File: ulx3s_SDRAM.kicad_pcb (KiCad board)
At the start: 4 copper layers, 14 parts, among them IC4 STM32F769IIT6, IC7 IS42S16400J

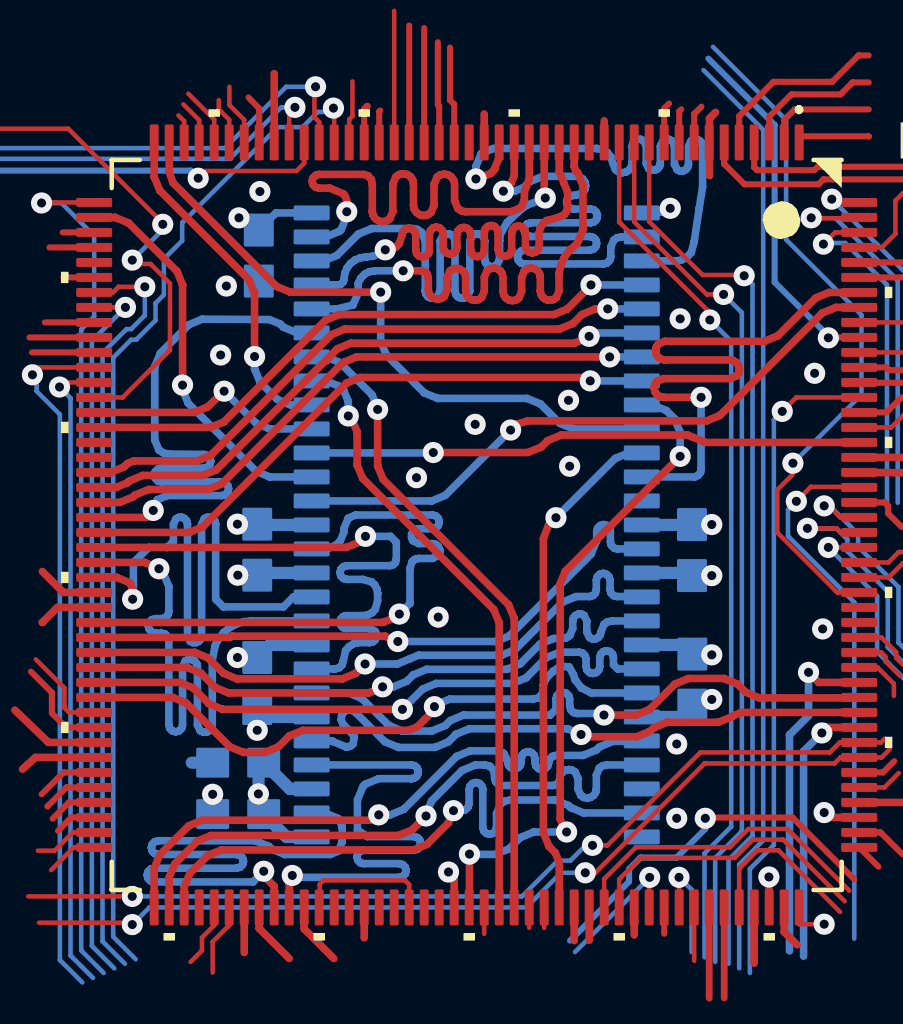
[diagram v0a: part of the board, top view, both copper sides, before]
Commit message: SDRAM footprint change
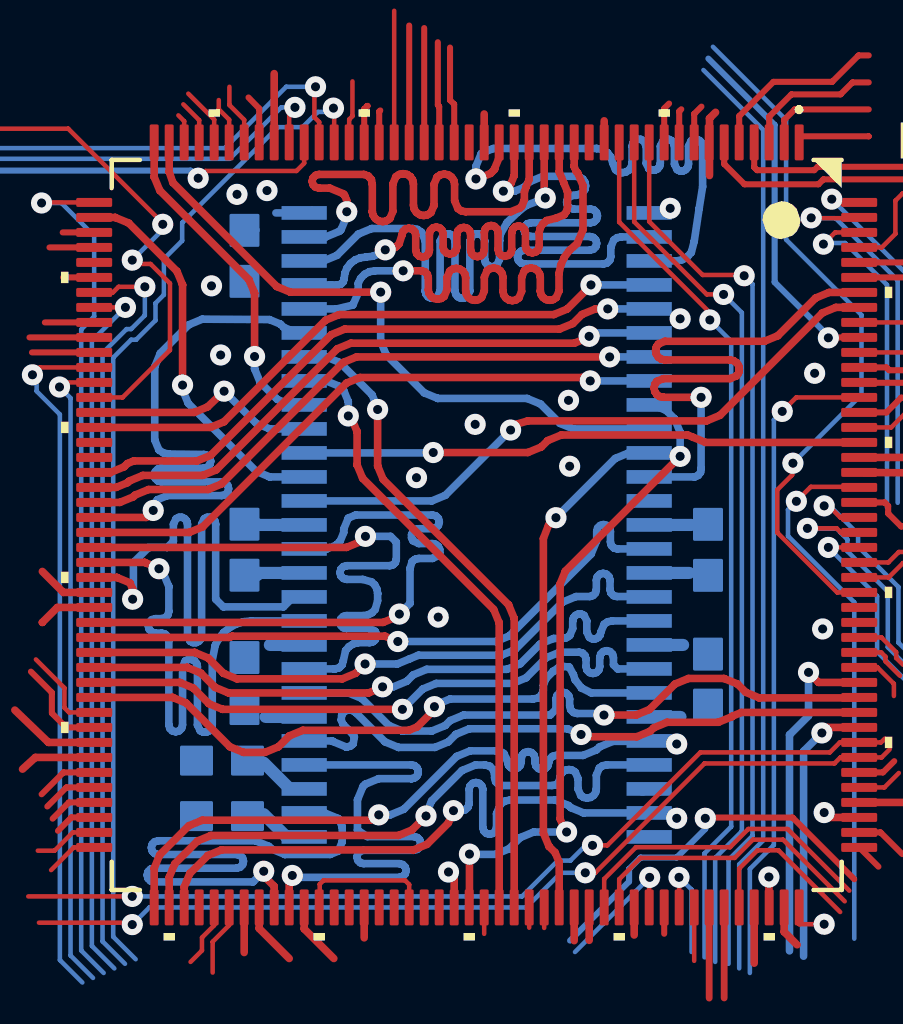
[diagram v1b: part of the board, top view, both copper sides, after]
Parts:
- IC7: footprint EEZ DIB MCU r3B4:TSOPII-54 -> Package_SO:TSOP-II-54_22.2x10.16mm_P0.8mm
- moved C49 0.54 mm to (0.08, 135.5)
- moved C43 0.54 mm to (0.08, 137.3)
- moved C47 0.53 mm to (16.3, 128.5)
- moved C48 0.52 mm to (16.3, 132.8)
- moved C46 0.48 mm to (0.83, 118.7)
- moved C44 0.42 mm to (0.83, 132.9)
- moved C45 0.42 mm to (0.83, 128.5)
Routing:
- net +3V3: track 43.0 -> 36.1 mm, vias 8 -> 3
- net GND: track 30.1 -> 25.2 mm, vias 22 -> 17

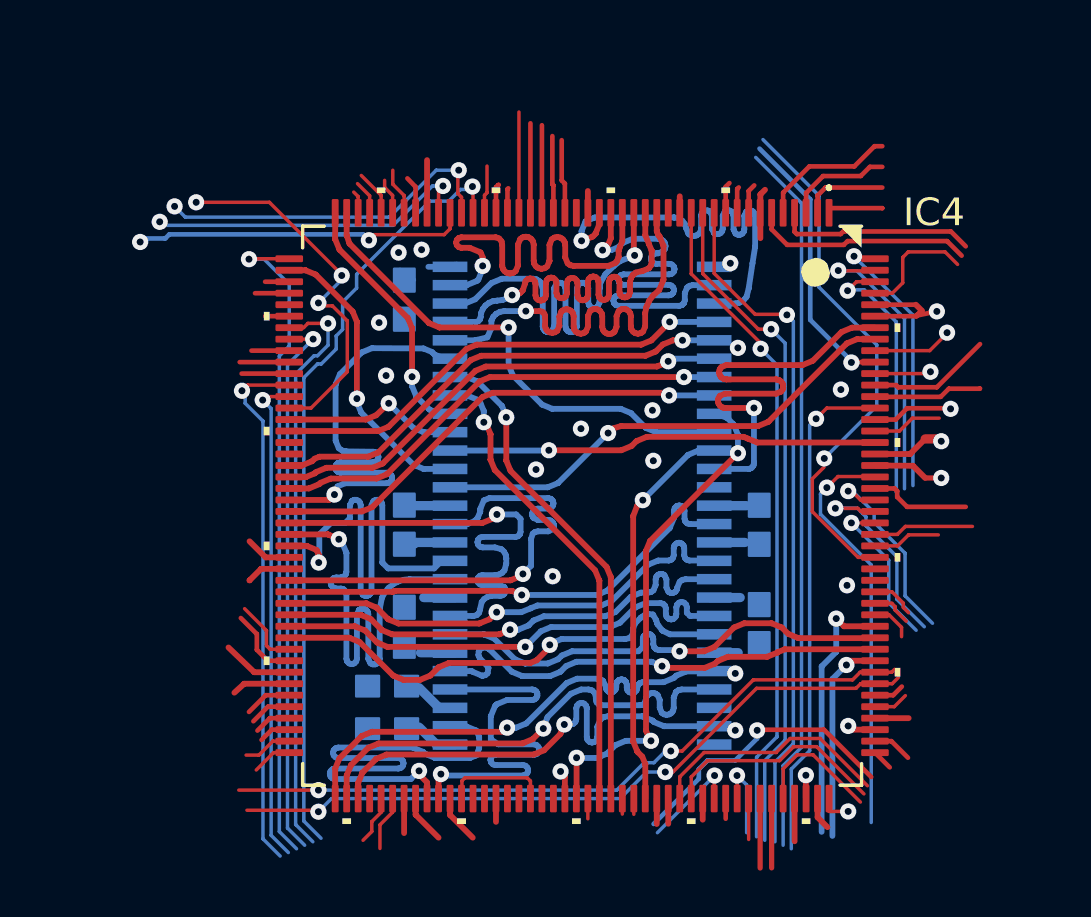
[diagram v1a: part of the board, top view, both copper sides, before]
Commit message: STM32 footprint change
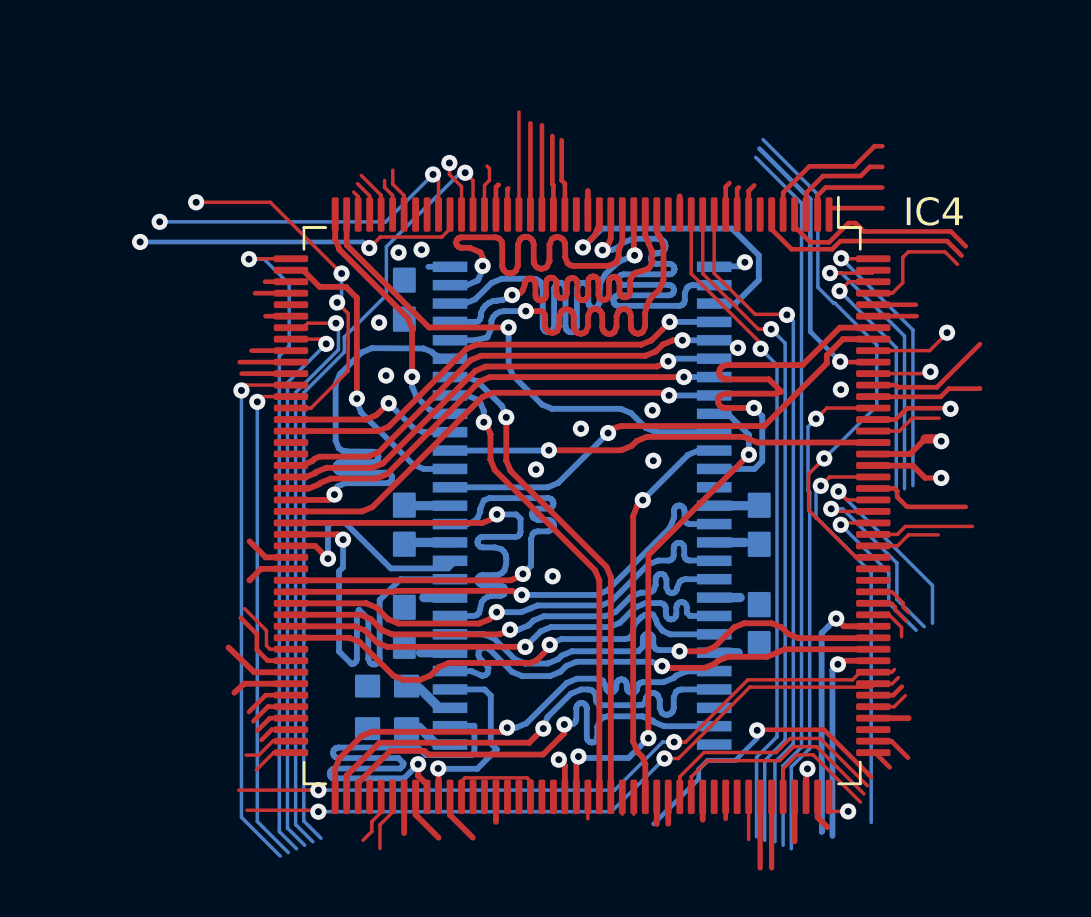
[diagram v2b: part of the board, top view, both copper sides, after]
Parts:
- IC4: footprint EEZ DIB MCU r3B4:LQFP-176_24X24MM -> Package_QFP:LQFP-176_24x24mm_P0.5mm
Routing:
- net ETH_MDC: track 15.4 -> 2.39 mm, vias 2 -> 1
- net FMC_D6: track 20.8 -> 10.1 mm
- net FMC_D1: track 18.9 -> 8.33 mm
- net FMC_A5: track 20.1 -> 14.0 mm
- net +3V3: track 36.1 -> 30.7 mm, vias 3 -> 2
- net MCLK_25: track 4.53 -> 0.00 mm, vias 1 -> 0
- net GND: track 25.2 -> 21.5 mm, vias 17 -> 14
- net USB_OTG_FS_VBUS: track 3.67 -> 0.00 mm, vias 1 -> 0
- net ~FAULT: track 16.3 -> 15.4 mm
- net FMC_D5: track 20.8 -> 20.0 mm
- net LTDC_G2: track 23.8 -> 24.5 mm
- net LTDC_B7: track 12.0 -> 12.7 mm
- net LTDC_G3: track 6.87 -> 7.47 mm
- net FMC_SDNWE: track 13.0 -> 13.6 mm
- net LTDC_R5: track 33.7 -> 34.2 mm
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
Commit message: Partial copied SDRAM routing from BB3
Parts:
- removed C47: 100n, EEZ DIB MCU r3B4:C0603
- removed IC4: STM32F769IIT6, Package_QFP:LQFP-176_24x24mm_P0.5mm
- removed IC7: IS42S16400J, Package_SO:TSOP-II-54_22.2x10.16mm_P0.8mm
- added B101: DS1092-10-W6L, EEZ DIB MCU r3B4:DS1092-10-W6L, F.Cu at (241.3, 39.5)
- added C1: 22uF, Capacitor_SMD:C_0805_2012Metric, B.Cu at (197.5, 75.9)
- added C10: 470pF, Capacitor_SMD:C_0603_1608Metric, B.Cu at (191.9, 76.7)
- added C101: N.C., Capacitor_SMD:C_0805_2012Metric, F.Cu at (139.9, 61.8)
- added C102: EEEFK1V220R, EEZ DIB MCU r3B4:PANASONIC_C, F.Cu at (249.8, 99.0)
- added C103: 2u2, Capacitor_SMD:C_0805_2012Metric, F.Cu at (252.7, 62.4)
- added C104: 10n, Capacitor_SMD:C_0805_2012Metric, F.Cu at (254.8, 111.1)
- added C105: 100n, Capacitor_SMD:C_0603_1608Metric, F.Cu at (169.4, 109.5)
- added C106: 10n, Capacitor_SMD:C_0805_2012Metric, F.Cu at (235.1, 106.1)
- added C107: 100n, Capacitor_SMD:C_0603_1608Metric, F.Cu at (168.9, 102.3)
- added C108: 10n, Capacitor_SMD:C_0805_2012Metric, F.Cu at (232.4, 106.1)
- added C109: 10n, Capacitor_SMD:C_0805_2012Metric, F.Cu at (241.0, 106.1)
- added C11: 22uF, Capacitor_SMD:C_0805_2012Metric, B.Cu at (191.9, 73.5)
- added C110: 100n, Capacitor_SMD:C_0603_1608Metric, F.Cu at (242.8, 105.8)
- added C111: 33p, Capacitor_SMD:C_0603_1608Metric, F.Cu at (160.0, 63.5)
- added C112: 4p7, Capacitor_SMD:C_0603_1608Metric, F.Cu at (171.3, 63.5)
- added C113: 33p, Capacitor_SMD:C_0603_1608Metric, F.Cu at (156.6, 63.5)
- added C114: 4p7, Capacitor_SMD:C_0603_1608Metric, F.Cu at (168.1, 63.5)
- added C115: EEEFK1V220R, EEZ DIB MCU r3B4:PANASONIC_C, F.Cu at (138.8, 107.4)
- added C116: 100n, Capacitor_SMD:C_0603_1608Metric, F.Cu at (144.2, 107.9)
- added C117: 100n, Capacitor_SMD:C_0603_1608Metric, B.Cu at (165.5, 63.8)
- added C118: 100n, Capacitor_SMD:C_0603_1608Metric, F.Cu at (179.8, 71.1)
- added C119: 100n, Capacitor_SMD:C_0603_1608Metric, F.Cu at (179.0, 78.6)
- added C12: 22uF, Capacitor_SMD:C_0805_2012Metric, B.Cu at (191.9, 71.6)
- added C120: 100n, Capacitor_SMD:C_0603_1608Metric, F.Cu at (183.3, 84.0)
- added C121: 100n, Capacitor_SMD:C_0603_1608Metric, F.Cu at (183.2, 90.4)
- added C122: 100n, Capacitor_SMD:C_0603_1608Metric, F.Cu at (176.9, 95.9)
- added C123: 100n, Capacitor_SMD:C_0603_1608Metric, F.Cu at (187.9, 59.3)
- added C124: 100n, Capacitor_SMD:C_0603_1608Metric, F.Cu at (165.2, 96.4)
- added C125: 1u, Capacitor_SMD:C_0805_2012Metric, F.Cu at (165.2, 98.2)
- added C126: 100n, Capacitor_SMD:C_0603_1608Metric, F.Cu at (158.4, 99.2)
- added C127: 100n, Capacitor_SMD:C_0603_1608Metric, F.Cu at (155.2, 99.2)
- added C128: 100n, Capacitor_SMD:C_0603_1608Metric, F.Cu at (141.9, 89.3)
- added C129: 100n, Capacitor_SMD:C_0603_1608Metric, F.Cu at (142.5, 83.6)
- added C13: 2.2uF, Capacitor_SMD:C_0805_2012Metric, F.Cu at (203.1, 69.9)
- added C130: 100n, Capacitor_SMD:C_0603_1608Metric, F.Cu at (142.4, 79.9)
- added C131: 100n, Capacitor_SMD:C_0603_1608Metric, B.Cu at (154.1, 64.4)
- added C132: 2u2, Capacitor_SMD:C_0805_2012Metric, F.Cu at (150.6, 109.0)
- added C133: 2u2, Capacitor_SMD:C_0805_2012Metric, B.Cu at (163.0, 63.9)
- added C134: 100n, Capacitor_SMD:C_0603_1608Metric, F.Cu at (143.6, 75.3)
- added C135: 1u, Capacitor_SMD:C_0805_2012Metric, F.Cu at (143.4, 73.5)
- added C136: 1u, Capacitor_SMD:C_0805_2012Metric, F.Cu at (151.0, 62.4)
- added C137: 100n, Capacitor_SMD:C_0603_1608Metric, F.Cu at (147.5, 62.4)
- added C138: 2u2, Capacitor_SMD:C_0805_2012Metric, F.Cu at (172.9, 97.7)
- added C139: 2u2, Capacitor_SMD:C_0805_2012Metric, F.Cu at (141.5, 87.3)
- added C140: N.C., Capacitor_SMD:C_0603_1608Metric, B.Cu at (232.4, 50.8)
- added C141: 4u7, Capacitor_SMD:C_1206_3216Metric, B.Cu at (179.3, 119.2)
- added C142: 100n, Capacitor_SMD:C_0603_1608Metric, B.Cu at (183.2, 80.4)
- added C143: 100n, Capacitor_SMD:C_0603_1608Metric, B.Cu at (87.5, 93.2)
- added C144: 100n, Capacitor_SMD:C_0603_1608Metric, B.Cu at (88.2, 88.9)
- added C145: 100n, Capacitor_SMD:C_0603_1608Metric, B.Cu at (88.2, 84.4)
- added C146: 100n, Capacitor_SMD:C_0603_1608Metric, B.Cu at (88.3, 74.6)
- added C147: 100n, Capacitor_SMD:C_0603_1608Metric, B.Cu at (103.6, 84.5)
- added C148: 100n, Capacitor_SMD:C_0603_1608Metric, B.Cu at (103.6, 88.8)
- added C149: 100n, Capacitor_SMD:C_0603_1608Metric, B.Cu at (87.5, 91.5)
- added C150: 4u7, Capacitor_SMD:C_1206_3216Metric, F.Cu at (132.6, 98.6)
- added C151: 1u, Capacitor_SMD:C_0805_2012Metric, F.Cu at (180.0, 103.6)
- added C152: 4u7, Capacitor_Tantalum_SMD:CP_EIA-3216-10_Kemet-I, F.Cu at (218.9, 106.5)
- added C153: 2u2, Capacitor_SMD:C_0805_2012Metric, F.Cu at (182.4, 103.6)
- added C154: 4n7/1kV, Capacitor_SMD:C_1812_4532Metric, F.Cu at (219.1, 121.1)
- added C155: 100n, Capacitor_SMD:C_0603_1608Metric, F.Cu at (212.0, 112.4)
- added C156: 4u7, Capacitor_SMD:C_1206_3216Metric, F.Cu at (195.6, 39.0)
- added C157: 100n, Capacitor_SMD:C_0603_1608Metric, F.Cu at (183.8, 96.2)
- added C158: 1u, Capacitor_SMD:C_0805_2012Metric, F.Cu at (183.8, 99.7)
- added C159: N.C., Capacitor_SMD:C_0603_1608Metric, F.Cu at (136.6, 44.1)
- added C160: 100n, Capacitor_SMD:C_0603_1608Metric, F.Cu at (153.2, 36.9)
- added C161: 100n, Capacitor_SMD:C_0603_1608Metric, F.Cu at (134.6, 45.2)
- added C162: 100n, Capacitor_SMD:C_0603_1608Metric, F.Cu at (158.9, 37.1)
- added C163: 100n, Capacitor_SMD:C_0603_1608Metric, F.Cu at (134.8, 36.7)
- added C164: 100n, Capacitor_SMD:C_0603_1608Metric, F.Cu at (156.8, 53.6)
- added C165: 100n, Capacitor_SMD:C_0603_1608Metric, F.Cu at (147.4, 33.9)
- added C166: 10uF, Capacitor_Tantalum_SMD:CP_EIA-3216-10_Kemet-I, F.Cu at (148.1, 52.2)
- added C167: 100n, Capacitor_SMD:C_0603_1608Metric, F.Cu at (146.3, 48.9)
- added C168: 100n, Capacitor_SMD:C_0603_1608Metric, F.Cu at (143.8, 42.0)
- added C169: 100n, Capacitor_SMD:C_0603_1608Metric, F.Cu at (154.6, 53.6)
- added C17: 2.2uF, Capacitor_SMD:C_0805_2012Metric, B.Cu at (213.5, 89.7)
- added C170: 100n, Capacitor_SMD:C_0603_1608Metric, F.Cu at (160.5, 43.8)
- added C19: 2.2uF, Capacitor_SMD:C_0805_2012Metric, B.Cu at (213.5, 79.5)
- added C2: 470pF, Capacitor_SMD:C_0603_1608Metric, B.Cu at (229.9, 95.0)
- added C20: 2.2uF, Capacitor_SMD:C_0805_2012Metric, B.Cu at (213.5, 84.7)
- added C22: 2.2uF, Capacitor_SMD:C_0805_2012Metric, B.Cu at (230.4, 96.6)
- added C23: 2.2uF, Capacitor_SMD:C_0805_2012Metric, B.Cu at (194.7, 66.4)
- added C24: 2.2uF, Capacitor_SMD:C_0805_2012Metric, B.Cu at (225.3, 73.0)
- added C25: 22nF, Capacitor_SMD:C_0603_1608Metric, B.Cu at (215.9, 84.3)
- added C26: 22nF, Capacitor_SMD:C_0603_1608Metric, B.Cu at (211.1, 84.3)
- added C27: 22nF, Capacitor_SMD:C_0603_1608Metric, B.Cu at (211.9, 89.3)
- added C28: 22nF, Capacitor_SMD:C_0603_1608Metric, B.Cu at (215.1, 89.3)
- added C29: 22nF, Capacitor_SMD:C_0603_1608Metric, B.Cu at (217.0, 89.2)
- added C3: 22uF, Capacitor_SMD:C_0805_2012Metric, B.Cu at (230.1, 88.7)
- added C30: 22nF, Capacitor_SMD:C_0603_1608Metric, B.Cu at (209.9, 89.1)
- added C31: 22nF, Capacitor_SMD:C_0603_1608Metric, B.Cu at (211.1, 86.5)
- added C32: 22nF, Capacitor_SMD:C_0603_1608Metric, B.Cu at (215.9, 86.5)
- added C36: 220nF, Capacitor_SMD:C_0603_1608Metric, F.Cu at (225.4, 73.9)
- added C37: 220nF, Capacitor_SMD:C_0603_1608Metric, F.Cu at (226.8, 73.9)
- added C38: 220nF, Capacitor_SMD:C_0603_1608Metric, F.Cu at (215.2, 73.9)
- added C39: 220nF, Capacitor_SMD:C_0603_1608Metric, F.Cu at (218.0, 73.9)
- added C4: 22uF, Capacitor_SMD:C_0805_2012Metric, B.Cu at (230.1, 90.6)
- added C40: 220nF, Capacitor_SMD:C_0603_1608Metric, F.Cu at (220.8, 73.9)
- added C41: 220nF, Capacitor_SMD:C_0603_1608Metric, F.Cu at (224.0, 73.9)
- added C42: 220nF, Capacitor_SMD:C_0603_1608Metric, F.Cu at (213.8, 73.9)
- added C5: 22uF, Capacitor_SMD:C_0805_2012Metric, B.Cu at (238.4, 90.0)
- added C50: 22nF, Capacitor_SMD:C_0603_1608Metric, B.Cu at (238.2, 82.7)
- added C51: 22nF, Capacitor_SMD:C_0603_1608Metric, B.Cu at (237.7, 96.3)
- added C53: 22nF, Capacitor_SMD:C_0603_1608Metric, B.Cu at (199.4, 83.1)
- added C6: 470pF, Capacitor_SMD:C_0603_1608Metric, B.Cu at (227.6, 80.5)
- added C7: 22uF, Capacitor_SMD:C_0805_2012Metric, B.Cu at (227.6, 77.3)
- added C8: 22uF, Capacitor_SMD:C_0805_2012Metric, B.Cu at (227.6, 75.4)
- added C9: 22uF, Capacitor_SMD:C_0805_2012Metric, B.Cu at (235.8, 76.7)
- added D101: SMBJ5.0A-TR, EEZ DIB MCU r3B4:DO214AA, F.Cu at (139.8, 68.9)
- added D102: RB751V40T1G, EEZ DIB MCU r3B4:SOD323-R, F.Cu at (178.0, 103.2)
- added D20: 3.6V, Diode_SMD:D_SOD-323, B.Cu at (201.4, 39.9)
- added D21: 3.6V, Diode_SMD:D_SOD-323, B.Cu at (207.6, 39.8)
- added D23: 1N914, Diode_SMD:D_SOD-323, B.Cu at (202.4, 43.3)
- added D24: 1N914, Diode_SMD:D_SOD-323, B.Cu at (200.4, 43.3)
- added D25: 1N914, Diode_SMD:D_SOD-323, B.Cu at (206.6, 43.1)
- added D26: 1N914, Diode_SMD:D_SOD-323, B.Cu at (208.5, 43.1)
- added D28: 1N914, Diode_SMD:D_SOD-323, B.Cu at (230.4, 82.3)
- added D29: 1N914, Diode_SMD:D_SOD-323, B.Cu at (230.4, 84.1)
- added D9: 0, jumper:D_SMA_Jumper_NC, B.Cu at (202.9, 47.4)
- added FM1: FIDUCIAL, EEZ DIB MCU r3B4:FIDUCIAL, F.Cu at (263.5, 111.0)
- added FM2: FIDUCIAL, EEZ DIB MCU r3B4:FIDUCIAL, F.Cu at (130.5, 116.0)
- added FM3: FIDUCIAL, EEZ DIB MCU r3B4:FIDUCIAL, F.Cu at (131.0, 35.4)
- added FM4: FIDUCIAL, EEZ DIB MCU r3B4:FIDUCIAL, F.Cu at (263.4, 35.7)
- added GND1: PCB_TEST_TABSHIELD, EEZ DIB MCU r3B4:PCB_SHIELD_TAB, F.Cu at (222.2, 50.2)
- added GPDI1: GPDI-D, conn-fci:CONN-10029449-111RLF, F.Cu at (221.5, 40.0)
- added H1: HOLE, MountingHole:MountingHole_3.2mm_M3_ISO14580_Pad, F.Cu at (131.0, 57.5)
- added H2: HOLE, MountingHole:MountingHole_3.2mm_M3_ISO14580_Pad, F.Cu at (249.9, 57.5)
- added H3: HOLE, MountingHole:MountingHole_3.2mm_M3_ISO14580_Pad, F.Cu at (249.9, 120.5)
- added H4: HOLE, MountingHole:MountingHole_3.2mm_M3_ISO14580_Pad, F.Cu at (130.8, 120.5)
- added IC101: TPD4E001DRLR, EEZ DIB MCU r3B4:DRL6, F.Cu at (167.9, 111.5)
- added IC102: 74AUP1G74DC.125, EEZ DIB MCU r3B4:DCU8, F.Cu at (245.2, 106.1)
- added IC103: CD74HC4050PWR, EEZ DIB MCU r3B4:PW16, F.Cu at (157.2, 104.8)
- added IC104: STM32F769IIT6, Package_QFP:LQFP-176_24x24mm_P0.5mm, F.Cu at (95.9, 83.6)
- added IC105: LD1117ADT33TR, EEZ DIB MCU r3B4:DPACK, F.Cu at (145.8, 115.7)
- added IC106: N.C., EEZ DIB MCU r3B4:DRL6, B.Cu at (179.9, 57.2)
- added IC107: IS42S16400J, Package_SO:TSOP-II-54_22.2x10.16mm_P0.8mm, B.Cu at (95.9, 83.6)
- added IC108: AT24C256C-SSHL-B, EEZ DIB MCU r3B4:SOIC127P600X173-8N, B.Cu at (185.2, 76.7)
- added IC109: TPS2051BDBVR, EEZ DIB MCU r3B4:DBV5, F.Cu at (218.5, 110.9)
- added IC110: TPS61169DCKR, EEZ DIB MCU r3B4:DCK5, F.Cu at (133.4, 94.0)
- added IC111: TPD4E001DRLR, EEZ DIB MCU r3B4:DRL6, F.Cu at (209.0, 110.5)
- added IC112: TSC2007IPW, EEZ DIB MCU r3B4:PW(R-PDSO-G16), B.Cu at (205.3, 104.7)
- added IC113: N.C., EEZ DIB MCU r3B4:DRL6, F.Cu at (160.8, 41.3)
- added IC114: DP83848CVV_NOPB, EEZ DIB MCU r3B4:PT48, F.Cu at (153.6, 45.8)
- added J101: 503398-1892, EEZ DIB MCU r3B4:5033981892, B.Cu at (182.5, 109.8)
- added J102: 67803-8020, EEZ DIB MCU r3B4:678038020, F.Cu at (209.0, 123.0)
- added J4: CONN_02X03, Socket_Strips:Socket_Strip_Straight_2x03, F.Cu at (216.0, 101.4)
- added JP101: JP2-NOCUT, EEZ DIB MCU r3B4:JP2-NOCUT, F.Cu at (176.0, 58.8)
- added JP102: JP2-NOCUT, EEZ DIB MCU r3B4:JP2-NOCUT, F.Cu at (174.1, 58.8)
- added JP103: JP2-CUT-0805, EEZ DIB MCU r3B4:R_0805, F.Cu at (232.2, 47.3)
- added JP104: JP2-CUT-0805, EEZ DIB MCU r3B4:R_0805, F.Cu at (251.0, 90.4)
- added JP105: JP2-CUT, EEZ DIB MCU r3B4:JP2-CUT, B.Cu at (177.4, 59.0)
- added JP106: JP3-CUT-0805-ROTATED, EEZ DIB MCU r3B4:JP3-0805-CUT2, F.Cu at (188.7, 115.7)
- added JP107: JP2-NOCUT-0805, EEZ DIB MCU r3B4:JP2-0805-NOCUT, F.Cu at (205.5, 111.4)
- added JP108: JP2-CUT, EEZ DIB MCU r3B4:JP2-CUT, F.Cu at (139.9, 43.0)
- added JP109: JP2-CUT, EEZ DIB MCU r3B4:JP2-CUT, F.Cu at (139.9, 44.9)
- added JP110: JP2-CUT, EEZ DIB MCU r3B4:JP2-CUT, F.Cu at (139.9, 41.0)
- added JP111: JP2-NOCUT, EEZ DIB MCU r3B4:JP2-NOCUT, F.Cu at (139.9, 46.9)
- added JP112: JP2-NOCUT, EEZ DIB MCU r3B4:JP2-NOCUT, F.Cu at (163.0, 45.1)
- added L1: 2.2uH, L_1008_1210:L_1008_1210, B.Cu at (233.9, 86.2)
- added L101: BLM18AG102SH1D, EEZ DIB MCU r3B4:BEAD0603, F.Cu at (147.4, 64.4)
- added L102: DLG-0403-4R7, EEZ DIB MCU r3B4:DE0403, F.Cu at (174.3, 103.4)
- added L103: BLM18AG102SH1D, EEZ DIB MCU r3B4:BEAD0603, F.Cu at (142.8, 38.4)
- added L2: 2.2uH, L_1008_1210:L_1008_1210, B.Cu at (196.3, 69.1)
- added L3: 2.2uH, L_1008_1210:L_1008_1210, B.Cu at (231.4, 72.9)
- added LABEL1: HR000002, EEZ DIB MCU r3B4:CERT-SMALL-SILK, F.Cu at (248.6, 74.0)
- added LCD101: 505110-4091, EEZ DIB MCU r3B4:FPC_40, F.Cu at (189.6, 110.3)
- added LED101: N.C., EEZ DIB MCU r3B4:LED_0805, F.Cu at (222.7, 117.8)
- added LED102: N.C., EEZ DIB MCU r3B4:LED_0805, F.Cu at (190.2, 37.8)
- added Q101: N.C., EEZ DIB MCU r3B4:SOT23-BEC, F.Cu at (218.3, 115.6)
- added Q102: 2N7002, EEZ DIB MCU r3B4:SOT103P240X110-3N, F.Cu at (198.6, 52.4)
- added R101: 4K7, Resistor_SMD:R_0603_1608Metric, F.Cu at (228.5, 106.1)
- added R102: 10K, Resistor_SMD:R_0603_1608Metric, F.Cu at (230.5, 106.1)
- added R103: 10K, Resistor_SMD:R_0603_1608Metric, F.Cu at (249.9, 106.1)
- added R104: 4K7, Resistor_SMD:R_0603_1608Metric, F.Cu at (164.2, 107.4)
- added R105: 4K7, Resistor_SMD:R_0603_1608Metric, F.Cu at (164.2, 103.5)
- added R106: 1K, Resistor_SMD:R_0603_1608Metric, F.Cu at (141.9, 96.4)
- added R107: 4K7, Resistor_SMD:R_0603_1608Metric, F.Cu at (237.0, 106.1)
- added R108: 4K7, Resistor_SMD:R_0603_1608Metric, F.Cu at (166.7, 107.4)
- added R109: 4K7, Resistor_SMD:R_0603_1608Metric, F.Cu at (166.7, 103.5)
- added R11: 10k, Resistor_SMD:R_0603_1608Metric, B.Cu at (192.7, 96.3)
- added R110: 1K, Resistor_SMD:R_0603_1608Metric, F.Cu at (141.9, 94.5)
- added R111: 10K, Resistor_SMD:R_0603_1608Metric, F.Cu at (239.0, 106.1)
- added R112: 4K7, Resistor_SMD:R_0603_1608Metric, F.Cu at (160.8, 46.9)
- added R113: 10K, Resistor_SMD:R_0603_1608Metric, F.Cu at (143.4, 71.5)
- added R114: N.C., Resistor_SMD:R_0603_1608Metric, F.Cu at (247.9, 106.1)
- added R115: 4K7, Resistor_SMD:R_0603_1608Metric, F.Cu at (144.0, 66.2)
- added R116: 1K5, Resistor_SMD:R_0805_2012Metric, F.Cu at (192.5, 58.1)
- added R117: 1K5, Resistor_SMD:R_0805_2012Metric, F.Cu at (192.7, 60.5)
- added R118: 47R, Resistor_SMD:R_0805_2012Metric, F.Cu at (151.0, 64.3)
- added R119: N.C., Resistor_SMD:R_0805_2012Metric, B.Cu at (180.1, 66.4)
- added R12: 10k, Resistor_SMD:R_0603_1608Metric, B.Cu at (191.6, 99.1)
- added R120: N.C., Resistor_SMD:R_0805_2012Metric, B.Cu at (180.7, 94.8)
- added R121: N.C., Resistor_SMD:R_0805_2012Metric, B.Cu at (183.4, 87.0)
- added R122: 47K, Resistor_SMD:R_0603_1608Metric, B.Cu at (199.6, 115.4)
- added R123: 47K, Resistor_SMD:R_0603_1608Metric, B.Cu at (199.6, 119.2)
- added R124: 10R, Resistor_SMD:R_0603_1608Metric, F.Cu at (133.1, 96.4)
- added R125: N.C., Resistor_SMD:R_0603_1608Metric, F.Cu at (222.7, 115.9)
- added R126: 10R, Resistor_SMD:R_0603_1608Metric, F.Cu at (133.4, 91.5)
- added R127: 10K, Resistor_SMD:R_0603_1608Metric, F.Cu at (222.7, 112.0)
- added R128: N.C., Resistor_SMD:R_0603_1608Metric, F.Cu at (222.7, 113.9)
- added R129: 4K7, Resistor_SMD:R_0805_2012Metric, F.Cu at (212.4, 108.6)
- added R130: 22R, Resistor_SMD:R_0805_2012Metric, F.Cu at (168.8, 98.1)
- added R131: 22R, Resistor_SMD:R_0805_2012Metric, F.Cu at (170.7, 98.1)
- added R132: 10K, Resistor_SMD:R_0603_1608Metric, F.Cu at (212.4, 110.6)
- added R133: 10K, Resistor_SMD:R_0603_1608Metric, F.Cu at (214.2, 105.3)
- added R134: 1K5, Resistor_SMD:R_0805_2012Metric, F.Cu at (144.5, 47.1)
- added R135: 49R9, Resistor_SMD:R_0805_2012Metric, F.Cu at (152.6, 33.4)
- added R136: 49R9, Resistor_SMD:R_0805_2012Metric, F.Cu at (156.0, 33.4)
- added R137: N.C., Resistor_SMD:R_0603_1608Metric, F.Cu at (130.6, 50.0)
- added R138: 2K2, Resistor_SMD:R_0805_2012Metric, F.Cu at (140.0, 53.6)
- added R139: 49R9, Resistor_SMD:R_0805_2012Metric, F.Cu at (155.1, 37.3)
- added R140: N.C., Resistor_SMD:R_0805_2012Metric, F.Cu at (131.0, 45.4)
- added R141: N.C., Resistor_SMD:R_0805_2012Metric, F.Cu at (190.1, 39.8)
- added R142: N.C., Resistor_SMD:R_0805_2012Metric, F.Cu at (131.0, 41.1)
- added R143: 2K2, Resistor_SMD:R_0805_2012Metric, F.Cu at (141.9, 53.6)
- added R144: 49R9, Resistor_SMD:R_0805_2012Metric, F.Cu at (157.1, 37.3)
- added R145: 2K2, Resistor_SMD:R_0805_2012Metric, F.Cu at (143.9, 53.6)
- added R146: 220R, Resistor_SMD:R_0603_1608Metric, F.Cu at (190.1, 33.9)
- added R147: 220R, Resistor_SMD:R_0603_1608Metric, F.Cu at (190.1, 35.9)
- added R148: 2K2, Resistor_SMD:R_0805_2012Metric, F.Cu at (135.7, 51.0)
- added R149: 2K2, Resistor_SMD:R_0805_2012Metric, F.Cu at (164.3, 50.9)
- added R150: 4K87, Resistor_SMD:R_0805_2012Metric, F.Cu at (147.7, 41.2)
- added R151: 2K2, Resistor_SMD:R_0805_2012Metric, F.Cu at (138.2, 35.7)
- added R27: 10k, Resistor_SMD:R_0603_1608Metric, B.Cu at (204.1, 94.3)
- added R28: 10k, Resistor_SMD:R_0603_1608Metric, B.Cu at (192.7, 94.8)
- added R29: 1.1k, Resistor_SMD:R_0603_1608Metric, B.Cu at (189.8, 99.1)
- added R30: 4.7k, Resistor_SMD:R_0603_1608Metric, B.Cu at (192.8, 91.5)
- added R31: 15k, Resistor_SMD:R_0603_1608Metric, B.Cu at (233.4, 82.4)
- added R32: 15k, Resistor_SMD:R_0603_1608Metric, B.Cu at (207.9, 95.7)
- added R33: 15k, Resistor_SMD:R_0603_1608Metric, B.Cu at (206.0, 95.7)
- added R40: 1.1k, Resistor_SMD:R_0603_1608Metric, B.Cu at (201.4, 37.0)
- added R52: 27, Resistor_SMD:R_0603_1608Metric, B.Cu at (205.2, 38.4)
- added R53: 27, Resistor_SMD:R_0603_1608Metric, B.Cu at (203.8, 38.4)
- added R54: 1.1k, Resistor_SMD:R_0603_1608Metric, B.Cu at (207.5, 36.8)
- added R61: 549, Resistor_SMD:R_0603_1608Metric, B.Cu at (223.2, 68.2)
- added R63: 15k, Resistor_SMD:R_0603_1608Metric, B.Cu at (201.4, 38.4)
- added R64: 15k, Resistor_SMD:R_0603_1608Metric, B.Cu at (207.5, 38.1)
- added RA1: 15k, Resistor_SMD:R_0603_1608Metric, B.Cu at (229.9, 93.7)
- added RA2: 15k, Resistor_SMD:R_0603_1608Metric, B.Cu at (191.9, 75.4)
- added RA3: 15k, Resistor_SMD:R_0603_1608Metric, B.Cu at (227.6, 79.2)
- added RB1: 18k, Resistor_SMD:R_0603_1608Metric, B.Cu at (233.3, 90.0)
- added RB2: 4.7k, Resistor_SMD:R_0603_1608Metric, B.Cu at (195.1, 72.9)
- added RB3: 3.3k, Resistor_SMD:R_0603_1608Metric, B.Cu at (230.7, 76.7)
- added RN101: DR1206-33R-4/8, EEZ DIB MCU r3B4:CAY16, F.Cu at (184.3, 66.4)
- added RN102: DR1206-33R-4/8, EEZ DIB MCU r3B4:CAY16, F.Cu at (184.2, 62.8)
- added RN103: DR1206-33R-4/8, EEZ DIB MCU r3B4:CAY16, F.Cu at (150.4, 99.9)
- added RN104: DR1206-33R-4/8, EEZ DIB MCU r3B4:CAY16, F.Cu at (144.4, 58.2)
- added RN105: DR1206-33R-4/8, EEZ DIB MCU r3B4:CAY16, F.Cu at (148.5, 58.2)
- added RN106: DR1206-33R-4/8, EEZ DIB MCU r3B4:CAY16, F.Cu at (152.3, 58.2)
- added RN107: DR1206-33R-4/8, EEZ DIB MCU r3B4:CAY16, F.Cu at (162.3, 54.2)
- added RN3: DR1206-33R-4/8, EEZ DIB MCU r3B4:CAY16, F.Cu at (180.9, 98.3)
- added RP1: 0, jumper:R_0805_2012Metric_Pad1.29x1.40mm_HandSolder_Jumper_NC, B.Cu at (227.3, 95.5)
- added RP2: 0, jumper:R_0805_2012Metric_Pad1.29x1.40mm_HandSolder_Jumper_NC, B.Cu at (191.6, 68.2)
- added RP3: 0, jumper:R_0805_2012Metric_Pad1.29x1.40mm_HandSolder_Jumper_NC, B.Cu at (224.5, 76.4)
- added SH101: SHORTNOHOLE, EEZ DIB MCU r3B4:SHORT_NOHOLE, F.Cu at (188.3, 42.7)
- added SP101: LD-BZEN 0903, EEZ DIB MCU r3B4:LD-BZEN-0903, F.Cu at (193.0, 46.6)
- added SW101: TL1100CF160Q, EEZ DIB MCU r3B4:TL1100C, F.Cu at (259.5, 119.8)
- added SW102: PEC16-2215F-S0024, EEZ DIB MCU r3B4:PEC16-2215F, F.Cu at (235.5, 116.4)
- added U1: LFE5U-85F-6BG381C, lfe5bg381:BGA-381_pitch0.8mm_dia0.4mm, F.Cu at (213.5, 85.9)
- added U10: IS25LP128F-JBLE, SOA008-150mil:SOA008-150-208mil, B.Cu at (197.1, 96.2)
- added U3: TLV62569DBV, TSOT-25:TSOT-25, B.Cu at (235.8, 90.0)
- added U4: TLV62569DBV, TSOT-25:TSOT-25, B.Cu at (197.6, 72.9)
- added U5: TLV62569DBV, TSOT-25:TSOT-25, B.Cu at (233.3, 76.8)
- added US2: MICRO_USB, usb_otg:USB-MICRO-B-FCI-10118192-0001LF, F.Cu at (204.2, 34.6)
- added X101: DS1024-2*20R0, EEZ DIB MCU r3B4:ZL263-40DG, F.Cu at (255.0, 56.5)
- added X102: DS1013-16SSIB1, EEZ DIB MCU r3B4:IDC-16PIN, F.Cu at (133.1, 75.2)
- added X103: 691322110005, EEZ DIB MCU r3B4:MC1,5_5-G-3,5, F.Cu at (166.2, 115.0)
- added X104: N.C., EEZ DIB MCU r3B4:SSW-106-02-S-S, F.Cu at (179.8, 55.0)
- added X105: LMJTAB881243M-L, EEZ DIB MCU r3B4:RJ45-TRAFO-LED, F.Cu at (175.7, 42.3)
- added Y1: FNETHE025, oscxo:Crystal_SMD_7050_4Pads, F.Cu at (194.8, 87.0)
- added Y101: 25MHz, EEZ DIB MCU r3B4:HC-49_4H, F.Cu at (160.0, 58.9)
- added Y102: XTAL016178-85SMX, EEZ DIB MCU r3B4:85SMX, F.Cu at (169.7, 58.1)
- added ZD101: BZX384-B24.115, EEZ DIB MCU r3B4:SOD323-W, F.Cu at (174.8, 110.1)
- C43, C44, C45: value 100n -> 220nF; footprint EEZ DIB MCU r3B4:C0603 -> Capacitor_SMD:C_0603_1608Metric; moved to F.Cu
- C46: value 100n -> 2.2uF; footprint EEZ DIB MCU r3B4:C0603 -> Capacitor_SMD:C_0805_2012Metric
- C48, C49: value 100n -> 22nF; footprint EEZ DIB MCU r3B4:C0603 -> Capacitor_SMD:C_0603_1608Metric
- moved C45 228.4 mm to (222.6, 73.9), turned to 90 degrees
- moved C44 226.4 mm to (219.4, 73.9), turned to 90 degrees
- moved C43 225.7 mm to (216.6, 73.9), turned to 90 degrees
- moved C46 221.9 mm to (221.9, 99.7), turned to 0 degrees
- moved C49 205.1 mm to (202.0, 99.6)
- moved C48 189.4 mm to (197.8, 78.7), turned to 180 degrees
- moved EEZ_SIGNATURE 59.1 mm to (-24.1, 57.5)
- moved U$2 59.1 mm to (-18.5, 68.0)
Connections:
- C43 pad 1: +3V3 -> FPDI_D1+
- C43 pad 2: GND -> /gpdi/GPDI_D1+
- C44 pad 1: +3V3 -> FPDI_D0+
- C44 pad 2: GND -> /gpdi/GPDI_D0+
- C45 pad 1: +3V3 -> FPDI_CLK+
- C45 pad 2: GND -> /gpdi/GPDI_CLK+
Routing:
- net (no net): track 0.00 -> 348.6 mm, vias 0 -> 73
- net GND: track 21.5 -> 263.9 mm, vias 14 -> 211
- net +5V: track 0.00 -> 138.8 mm, vias 0 -> 1
- net +2V5: track 0.00 -> 97.0 mm, vias 0 -> 8
- net +3V3: track 30.7 -> 117.1 mm, vias 2 -> 43
- net +1V1: track 0.00 -> 68.4 mm, vias 0 -> 7
- net LTDC_TO_FPGA_G6: track 0.00 -> 41.7 mm, vias 0 -> 2
- net PE: track 0.00 -> 40.8 mm
- net LTDC_TO_FPGA_R5: track 0.00 -> 40.0 mm, vias 0 -> 2
- net LTDC_TO_FPGA_HSYNC: track 0.00 -> 36.3 mm, vias 0 -> 2
- net LTDC_TO_FPGA_VSYNC: track 0.00 -> 34.8 mm, vias 0 -> 1
- net 2V5_3V3: track 0.00 -> 34.2 mm, vias 0 -> 3
- net LTDC_R5: track 34.2 -> 0.00 mm, vias 1 -> 0
- net LTDC_TO_FPGA_G4: track 0.00 -> 33.1 mm, vias 0 -> 1
- net LTDC_TO_FPGA_G2: track 0.00 -> 31.6 mm, vias 0 -> 2
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- added copper zone on In1.Cu, net +1V1
- added copper zone on In1.Cu, net +2V5
- added copper zone on B.Cu, net +3V3
- added copper zone on F.Cu, net +3V3
- added copper zone on In1.Cu, net +3V3
- added copper zone on F.Cu, net +5V
- added copper zone on In2.Cu, net +5V
- added copper zone on In1.Cu, net 2V5_3V3
- added copper zone on B.Cu, net GND
- added copper zone on F.Cu, net GND
- added copper zone on In1.Cu, net GND
- added copper zone on In2.Cu, net GND
- added copper zone on F.Cu, net Net-(D2-PadA)
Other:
- board outline added: 139.5 x 91.8 mm
- net class BGA added: clearance 0.127, trace_width 0.127, via_dia 0.419, via_drill 0.2
- net class Default: clearance 0.1016 -> 0.127; trace_width 0.25 -> 0.3; via_dia 0.8 -> 0.419; via_drill 0.4 -> 0.2
- net class Medium added: clearance 0.127, trace_width 0.127, via_dia 0.419, via_drill 0.2
- rule pad_to_mask_clearance: 0.051 -> 0.05
- rule trace_clearance: 0.1016 -> 0.127
- rule via_min_size: 0.2032 -> 0.419
- board text added: "+1.1V"
- board text added: "+2.5V"
- board text added: "+3.3V"
- board text added: "1"
- board text added: "1 Vdd target 2 SWCLK 3 Gnd 4 SWDIO 5 !RESET! 6 SWO"
- board text added: "2"
- board text added: "3"
- board text added: "3V3"
- board text added: "4"
- board text added: "EEZ DIB MCU (10/2020 r3B4) Project source code: github.com/eez-open/modular-psu"
- board text added: "EEZ FPGA Proto (10/2020 r001)"
- board text added: "FLASH"
- board text added: "FPGA"
- board text added: "GND"
- board text added: "KEYSTONE 3000"
- board text added: "PRG"
- board text added: "TCK"
- board text added: "TDI"
- board text added: "TDO"
- board text added: "TMS"
- board text added: "ULX3S"
- board text added: "v3.1.3?"
